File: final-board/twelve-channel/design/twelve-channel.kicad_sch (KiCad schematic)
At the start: 8 parts, among them J49 Screw terminal 3-pos 5.08mm, J50 Screw terminal 3-pos 5.08mm (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

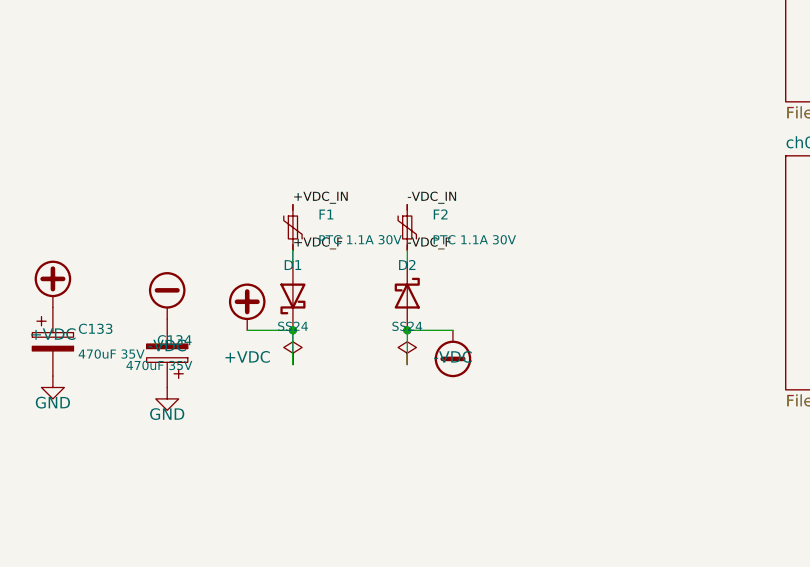
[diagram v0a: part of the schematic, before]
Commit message: 12ch BOM + verified protection MPNs
Regenerated models-bom/twelve-channel-bom.csv (gen_bom.py: groups the 464 netlist parts by
MPN/value/DNP, enriches from the single-channel BOM) = 23 line items, 344 FIT + 120 DNP.

Verified the up-rated common-power parts (SOURCING-VERIFICATION-2026-07-08) - all 3 provisional
picks rejected + replaced with in-stock parts (footprints unchanged, DRC still 0/0/0):
  PTC  MF-MSMF110-2 (obsolete + 6V) -> Littelfuse 1812L110/24DR  (1.1A/24V, 1812)
  Schk SS24 (SMB not SMA + obsolete) -> onsemi SSA24             (2A/40V, SMA)
  bulk UWT1V471MNL1GS (fictional)    -> Panasonic EEE-FN1V471UP  (470uF/35V, 10x10.5)
Sizing confirmed vs the 12ch current budget (per board +rail 384mA default / 584mA all-buffered;
1.1A PTC hold = ~1.9x margin). Also merged J_DAISY value with J_PWR so the 2 screw terminals
group as one BOM line.

Co-Authored-By: Claude Opus 4.8 <noreply@anthropic.com>
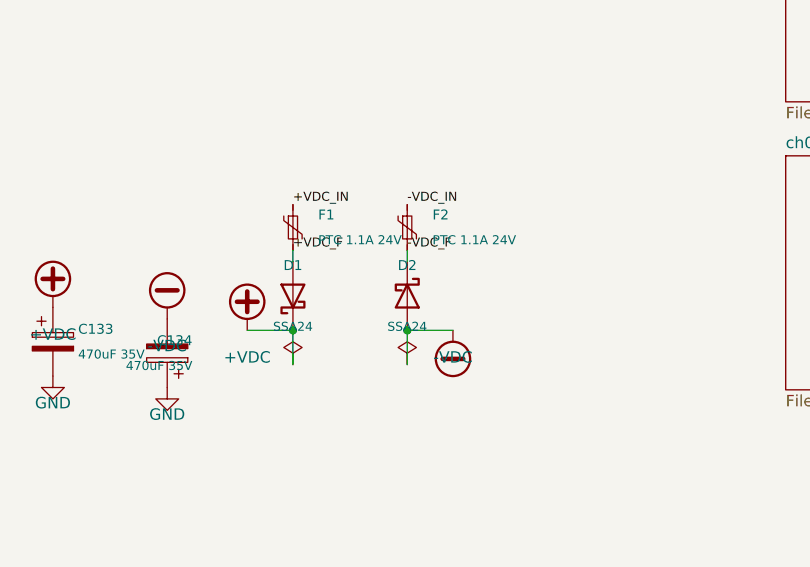
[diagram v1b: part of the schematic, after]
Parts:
- C133, C134: Distributor PN 493-13313-1-ND -> 10-EEE-FN1V471UPCT-ND; MPN UWT1V471MNL1GS -> EEE-FN1V471UP; Manufacturer Nichicon -> Panasonic
- D1, D2: value SS24 -> SSA24; Distributor PN SS24FSCT-ND -> SSA24CT-ND; MPN SS24 -> SSA24
- F1, F2: value PTC 1.1A 30V -> PTC 1.1A 24V; Distributor PN MF-MSMF110-2CT-ND -> F5632CT-ND; MPN MF-MSMF110-2 -> 1812L110/24DR; Manufacturer Bourns -> Littelfuse
- J50: value Screw terminal 3-pos 5.08mm (daisy) -> Screw terminal 3-pos 5.08mm
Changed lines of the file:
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@@
 			(effects (font (size 1.1 1.1)))
 		)
-		(property "Value" "Screw terminal 3-pos 5.08mm (daisy)"
+		(property "Value" "Screw terminal 3-pos 5.08mm"
 			(at 52.8 231.56 0)
 			(hide yes)
@@
 			(effects (font (size 1.1 1.1)) (justify left))
 		)
-		(property "Value" "PTC 1.1A 30V"
+		(property "Value" "PTC 1.1A 24V"
 			(at 98.05 189.36 0)
 			(effects (font (size 1.0 1.0)) (justify left))
@@
 			(effects (font (size 1.27 1.27)))
 		)
-		(property "MPN" "MF-MSMF110-2"
-			(at 95.25 187.96 0)
-			(hide yes)
-			(effects (font (size 1.27 1.27)))
-		)
-		(property "Manufacturer" "Bourns"
-			(at 95.25 187.96 0)
-			(hide yes)
-			(effects (font (size 1.27 1.27)))
-		)
-		(property "Distributor PN" "MF-MSMF110-2CT-ND"
+		(property "MPN" "1812L110/24DR"
+			(at 95.25 187.96 0)
+			(hide yes)
+			(effects (font (size 1.27 1.27)))
+		)
+		(property "Manufacturer" "Littelfuse"
+			(at 95.25 187.96 0)
+			(hide yes)
+			(effects (font (size 1.27 1.27)))
+		)
+		(property "Distributor PN" "F5632CT-ND"
 			(at 95.25 187.96 0)
 			(hide yes)
@@
 			(effects (font (size 1.1 1.1)))
 		)
-		(property "Value" "SS24"
+		(property "Value" "SSA24"
 			(at 95.25 198.98000000000002 90)
 			(effects (font (size 1.0 1.0)))
@@
 			(effects (font (size 1.27 1.27)))
 		)
-		(property "MPN" "SS24"
+		(property "MPN" "SSA24"
 			(at 95.25 195.58 0)
 			(hide yes)
@@
 			(effects (font (size 1.27 1.27)))
 		)
-		(property "Distributor PN" "SS24FSCT-ND"
+		(property "Distributor PN" "SSA24CT-ND"
 			(at 95.25 195.58 0)
 			(hide yes)
@@
 			(effects (font (size 1.1 1.1)) (justify left))
 		)
-		(property "Value" "PTC 1.1A 30V"
+		(property "Value" "PTC 1.1A 24V"
 			(at 110.75 189.36 0)
 			(effects (font (size 1.0 1.0)) (justify left))
@@
 			(effects (font (size 1.27 1.27)))
 		)
-		(property "MPN" "MF-MSMF110-2"
-			(at 107.95 187.96 0)
-			(hide yes)
-			(effects (font (size 1.27 1.27)))
-		)
-		(property "Manufacturer" "Bourns"
-			(at 107.95 187.96 0)
-			(hide yes)
-			(effects (font (size 1.27 1.27)))
-		)
-		(property "Distributor PN" "MF-MSMF110-2CT-ND"
+		(property "MPN" "1812L110/24DR"
+			(at 107.95 187.96 0)
+			(hide yes)
+			(effects (font (size 1.27 1.27)))
+		)
+		(property "Manufacturer" "Littelfuse"
+			(at 107.95 187.96 0)
+			(hide yes)
+			(effects (font (size 1.27 1.27)))
+		)
+		(property "Distributor PN" "F5632CT-ND"
 			(at 107.95 187.96 0)
 			(hide yes)
@@
 			(effects (font (size 1.1 1.1)))
 		)
-		(property "Value" "SS24"
+		(property "Value" "SSA24"
 			(at 107.95 198.98000000000002 90)
 			(effects (font (size 1.0 1.0)))
@@
 			(effects (font (size 1.27 1.27)))
 		)
-		(property "MPN" "SS24"
+		(property "MPN" "SSA24"
 			(at 107.95 195.58 0)
 			(hide yes)
@@
 			(effects (font (size 1.27 1.27)))
 		)
-		(property "Distributor PN" "SS24FSCT-ND"
+		(property "Distributor PN" "SSA24CT-ND"
 			(at 107.95 195.58 0)
 			(hide yes)
@@
 			(effects (font (size 1.27 1.27)))
 		)
-		(property "MPN" "UWT1V471MNL1GS"
-			(at 68.58 200.66 0)
-			(hide yes)
-			(effects (font (size 1.27 1.27)))
-		)
-		(property "Manufacturer" "Nichicon"
-			(at 68.58 200.66 0)
-			(hide yes)
-			(effects (font (size 1.27 1.27)))
-		)
-		(property "Distributor PN" "493-13313-1-ND"
+		(property "MPN" "EEE-FN1V471UP"
+			(at 68.58 200.66 0)
+			(hide yes)
+			(effects (font (size 1.27 1.27)))
+		)
+		(property "Manufacturer" "Panasonic"
+			(at 68.58 200.66 0)
+			(hide yes)
+			(effects (font (size 1.27 1.27)))
+		)
+		(property "Distributor PN" "10-EEE-FN1V471UPCT-ND"
 			(at 68.58 200.66 0)
 			(hide yes)
@@
 			(effects (font (size 1.27 1.27)))
 		)
-		(property "MPN" "UWT1V471MNL1GS"
-			(at 81.28 201.93 0)
-			(hide yes)
-			(effects (font (size 1.27 1.27)))
-		)
-		(property "Manufacturer" "Nichicon"
-			(at 81.28 201.93 0)
-			(hide yes)
-			(effects (font (size 1.27 1.27)))
-		)
-		(property "Distributor PN" "493-13313-1-ND"
-			(at 81.28 201.93 0)
-			(hide yes)
+		(property "MPN" "EEE-FN1V471UP"
+			(at 81.28 201.93 0)
+			(hide yes)
+			(effects (font (size 1.27 1.27)))
+		)
+		(property "Manufacturer" "Panasonic"
+			(at 81.28 201.93 0)
+			(hide yes)
+			(effects (font (size 1.27 1.27)))
+		)
+		(property "Distributor PN" "10-EEE-FN1V471UPCT-ND"
+			(at 81.28 201.93 0)
+			(hide yes)
